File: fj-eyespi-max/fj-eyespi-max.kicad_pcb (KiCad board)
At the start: 2 copper layers, 2 parts, among them J1 Conn_01x18_Socket, J2 Conn_02x16_Odd_Even

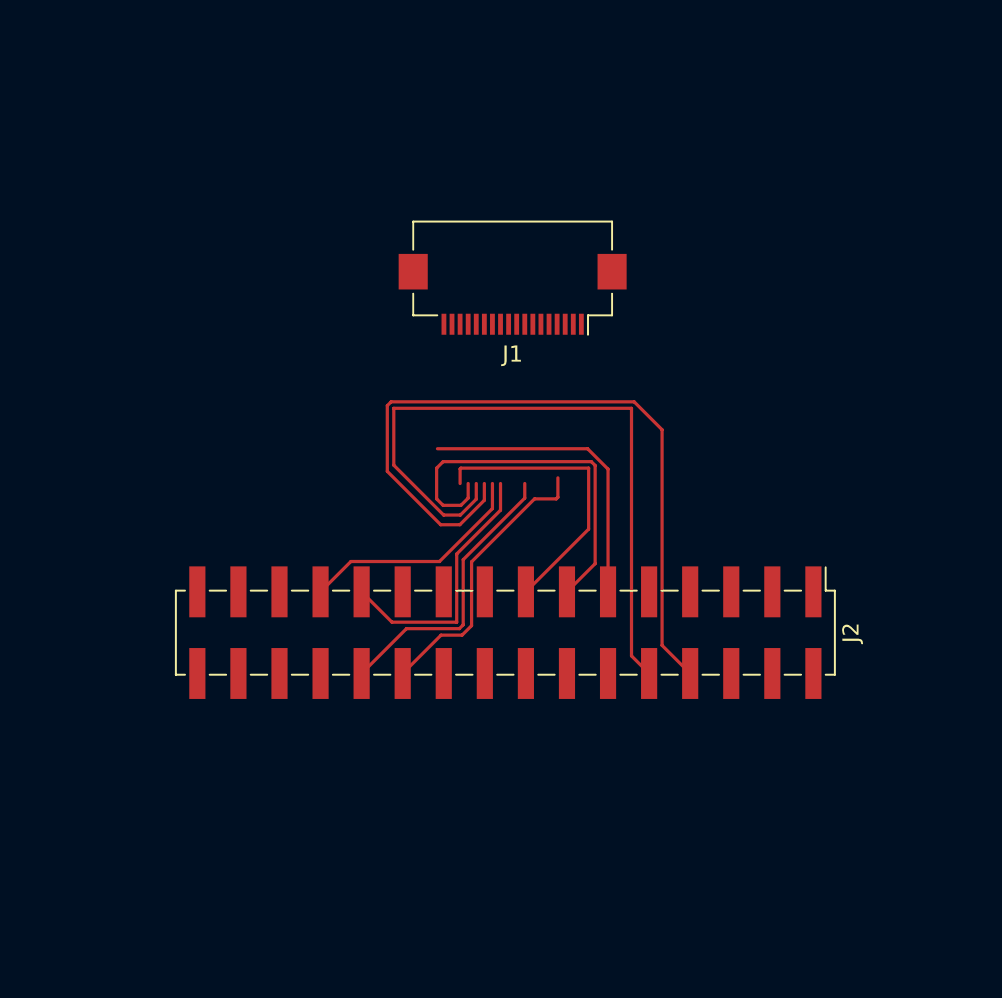
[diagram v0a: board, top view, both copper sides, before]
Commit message: total remix
min and max boards re-routed and date, new silks....
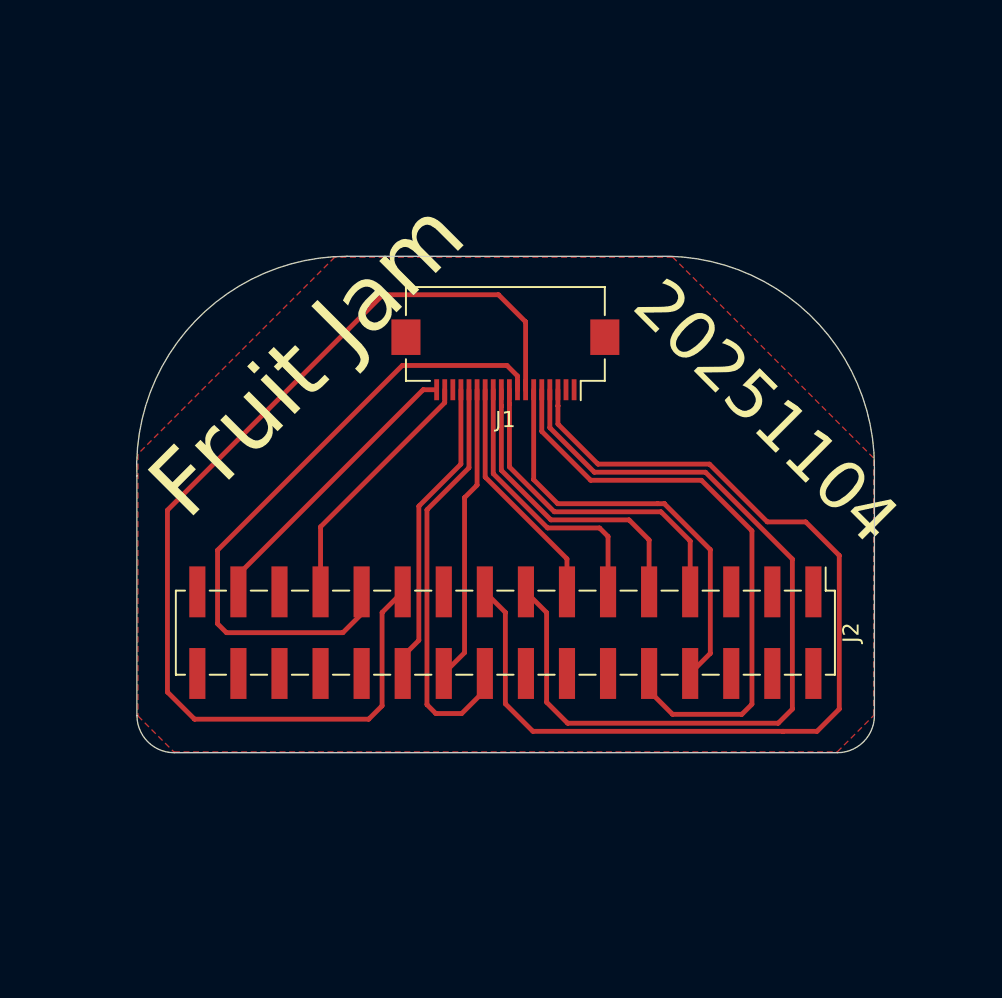
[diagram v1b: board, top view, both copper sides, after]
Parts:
- moved J1 4.07 mm to (156.0, 77.1)
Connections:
- net /disp_cs renamed /sdcs
- J1 pad 1: 3v3 -> /gpio2
- J1 pad 10: /sd_cs -> /tcs
- J1 pad 11: /mem_cs -> /rst
- J1 pad 12: /ts_cs -> /dc
- J1 pad 13: /scl -> /miso
- J1 pad 14: /sda -> /mosi
- J1 pad 15: /int -> /sck
- J1 pad 16: /busy -> gnd
- J1 pad 17: /gpio1 -> /lite
- J1 pad 18: /gpio2 -> 3v3
- J1 pad 2: /backlite -> /gpio1
- J1 pad 3: gnd -> /busy
- J1 pad 4: /sck -> /int
- J1 pad 5: /mosi -> /sda
- J1 pad 6: /miso -> /scl
- J1 pad 7: /dc -> /tscs
- J1 pad 8: /reset -> /mcs
- J2 pad 11: /gpio2 -> /rst
- J2 pad 13: /int -> /dc
- J2 pad 15: /busy -> /int
- J2 pad 17: /backlite -> /busy
- J2 pad 19: /dc -> unconnected-(J2-Pin_19-Pad19)
- J2 pad 21: /sd_cs -> /tscs
- J2 pad 23: /mem_cs -> /mcs
- J2 pad 24: /reset -> unconnected-(J2-Pin_24-Pad24)
- J2 pad 25: /ts_cs -> /lite
- J2 pad 27: unconnected-(J2-Pin_27-Pad27) -> gnd
- J2 pad 28: unconnected-(J2-Pin_28-Pad28) -> gnd
- J2 pad 29: unconnected-(J2-Pin_29-Pad29) -> 3v3
- J2 pad 3: 3v3 -> unconnected-(J2-Pin_3-Pad3)
- J2 pad 6: unconnected-(J2-Pin_6-Pad6) -> gnd
- J2 pad 9: /gpio1 -> /tcs
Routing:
- net /tscs: track 0.00 -> 65.7 mm
- net /busy: track 18.1 -> 61.8 mm
- net /mcs: track 0.00 -> 39.9 mm
- net /int: track 23.7 -> 53.4 mm
- net /mosi: track 0.00 -> 26.0 mm
- net /sdcs: track 0.00 -> 21.0 mm
- net /scl: track 46.7 -> 26.5 mm
- net /tcs: track 0.00 -> 19.1 mm
- net /gpio2: track 18.7 -> 0.00 mm
- net /miso: track 0.00 -> 18.4 mm
- net 3v3: track 0.00 -> 18.1 mm
- net /reset: track 17.8 -> 0.00 mm
- net /rst: track 0.00 -> 17.3 mm
- net /mem_cs: track 16.4 -> 0.00 mm
- net /lite: track 0.00 -> 15.7 mm
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- added copper zone on F.Cu, net gnd
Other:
- board outline added: 45.6 x 30.7 mm
- board text added: "20251104"
- board text added: "Fruit Jam"
- board text added: "Fruit Jam EYESPI MAX 20251104"

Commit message: re-routing
still had some flipped pins switching to max only
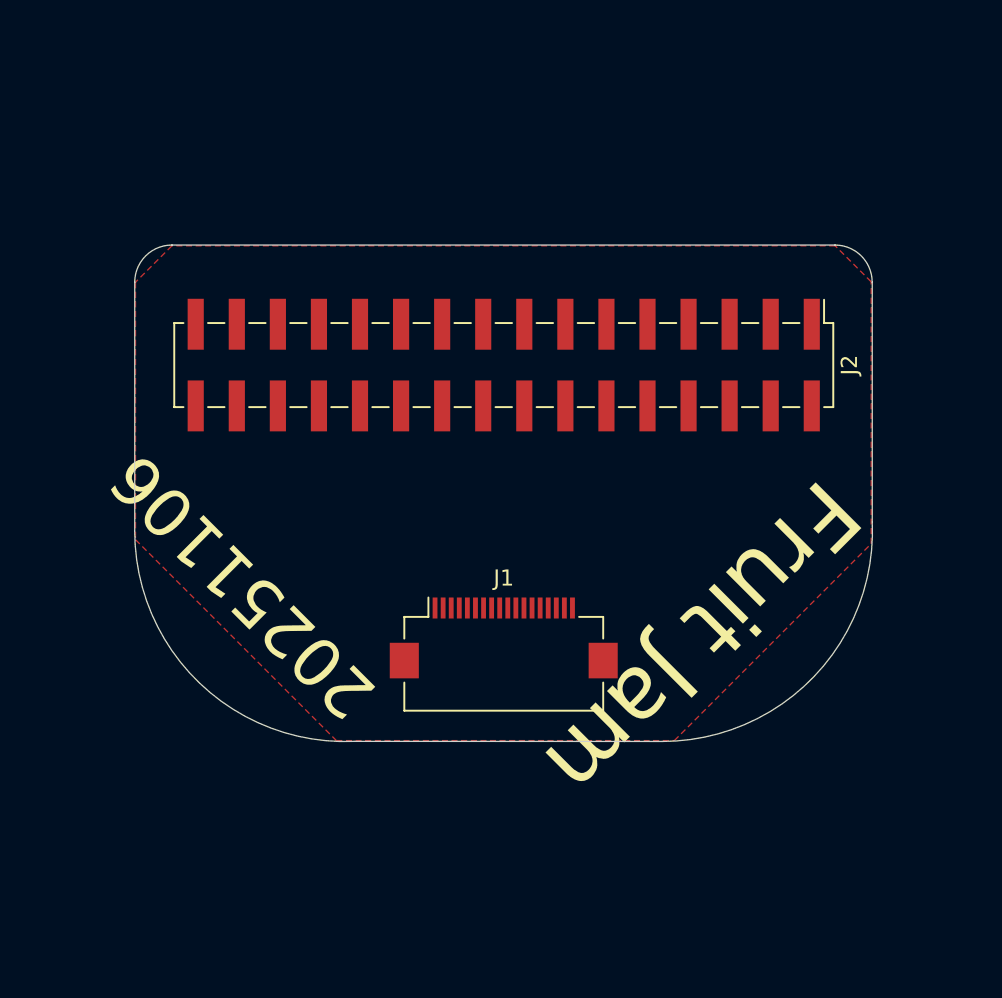
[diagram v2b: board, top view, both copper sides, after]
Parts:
- J2: value Conn_02x16_Odd_Even -> FruitJam-2x16
- moved J1 17.2 mm to (155.9, 94.3), turned to 0 degrees
- moved J2 16.6 mm to (155.9, 77.4)
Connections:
- J2 pad 10: /sda -> /dc
- J2 pad 11: /rst -> unconnected-(J2-Pin_11-Pad11)
- J2 pad 12: unconnected-(J2-Pin_12-Pad12) -> /rst
- J2 pad 13: /dc -> unconnected-(J2-Pin_13-Pad13)
- J2 pad 14: unconnected-(J2-Pin_14-Pad14) -> /tcs
- J2 pad 15: /int -> unconnected-(J2-Pin_15-Pad15)
- J2 pad 16: unconnected-(J2-Pin_16-Pad16) -> /sdcs
- J2 pad 17: /busy -> /mosi
- J2 pad 18: /mosi -> /int
- J2 pad 19: unconnected-(J2-Pin_19-Pad19) -> /miso
- J2 pad 20: /miso -> /busy
- J2 pad 21: /tscs -> /sck
- J2 pad 22: /sck -> /tscs
- J2 pad 23: /mcs -> unconnected-(J2-Pin_23-Pad23)
- J2 pad 24: unconnected-(J2-Pin_24-Pad24) -> /mcs
- J2 pad 25: /lite -> unconnected-(J2-Pin_25-Pad25)
- J2 pad 29: 3v3 -> unconnected-(J2-Pin_29-Pad29)
- J2 pad 30: unconnected-(J2-Pin_30-Pad30) -> 3v3
- J2 pad 7: /sdcs -> /scl
- J2 pad 8: /scl -> /lite
- J2 pad 9: /tcs -> /sda
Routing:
- net /tscs: track 65.7 -> 0.00 mm
- net /busy: track 61.8 -> 0.00 mm
- net /int: track 53.4 -> 0.00 mm
- net /mcs: track 39.9 -> 0.00 mm
- net /sda: track 37.1 -> 0.00 mm
- net /scl: track 26.5 -> 0.00 mm
- net /mosi: track 26.0 -> 0.00 mm
- net /sdcs: track 21.0 -> 0.00 mm
- net /tcs: track 19.1 -> 0.00 mm
- net /sck: track 19.0 -> 0.00 mm
- net /miso: track 18.4 -> 0.00 mm
- net 3v3: track 18.1 -> 0.00 mm
- net /rst: track 17.3 -> 0.00 mm
- net /lite: track 15.7 -> 0.00 mm
- net /dc: track 14.6 -> 0.00 mm
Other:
- outline, holes or cut-outs redrawn
- board text added: "20251106"
- board text removed: "20251104"

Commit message: re-routed max
aligned with flipped header
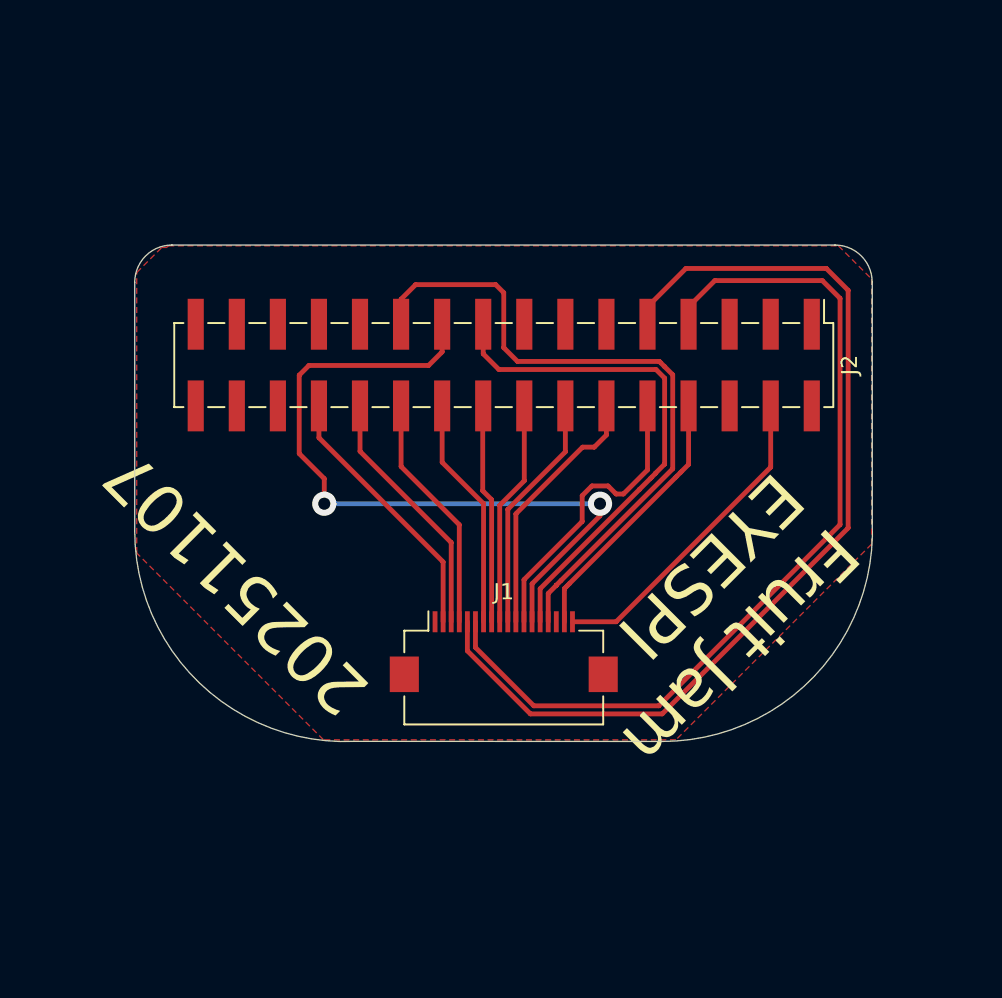
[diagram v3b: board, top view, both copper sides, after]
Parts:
- moved J1 0.85 mm to (155.9, 95.2)
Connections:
- J2 pad 18: /int -> /mcs
- J2 pad 20: /busy -> /tscs
- J2 pad 22: /tscs -> /int
- J2 pad 24: /mcs -> /busy
- J2 pad 26: unconnected-(J2-Pin_26-Pad26) -> /gpio1
- J2 pad 30: 3v3 -> unconnected-(J2-Pin_30-Pad30)
- J2 pad 4: unconnected-(J2-Pin_4-Pad4) -> 3v3
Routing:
- net /sda: track 0.00 -> 61.5 mm
- net /scl: track 0.00 -> 55.8 mm
- net /miso: track 0.00 -> 46.1 mm, vias 0 -> 2
- net /sck: track 0.00 -> 41.5 mm
- net /mosi: track 0.00 -> 31.9 mm
- net 3v3: track 0.00 -> 20.0 mm
- net /dc: track 0.00 -> 18.4 mm
- net /lite: track 0.00 -> 16.5 mm
- net /gpio1: track 0.00 -> 16.5 mm
- net /rst: track 0.00 -> 16.1 mm
- net /busy: track 0.00 -> 15.7 mm
- net /int: track 0.00 -> 14.8 mm
- net /tcs: track 0.00 -> 14.8 mm
- net /tscs: track 0.00 -> 14.4 mm
- net /sdcs: track 0.00 -> 14.0 mm
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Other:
- board text added: "20251107"
- board text added: "Fruit Jam EYESPI"
- board text added: "Fruit Jam EYESPI MAX 20251107"
- board text removed: "20251106"
- board text removed: "Fruit Jam"
- board text removed: "Fruit Jam EYESPI MAX 20251104"
